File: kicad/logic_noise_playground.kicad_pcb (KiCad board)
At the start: 2 copper layers, 200 x 100 mm, 160 parts, among them J2 SJ1-3524NG, P1 CONN_02X03, P10 CONN_01X03, P11 CONN_01X05, P12 CONN_02X04, P13 CONN_01X03, P14 CONN_01X02, P15 CONN_02X08, P16 CONN_01X04, P17 CONN_02X04, P18 CONN_01X04, P19 CONN_01X02, P2 CONN_01X02, P20 CONN_01X06, P21 CONN_02X03, P22 CONN_02X03, P23 CONN_01X02, P24 CONN_02X01, P25 CONN_01X02, P26 CONN_02X12, P27 CONN_01X02, P28 CONN_01X02, P29 CONN_01X02, P3 CONN_02X02, P30 CONN_01X02, P31 CONN_01X02, P32 CONN_01X03, P33 CONN_01X04, P34 CONN_01X04, P35 CONN_01X04, P36 CONN_01X04, P37 CONN_02X01, P38 CONN_01X04, P39 CONN_01X04, P4 CONN_02X06, P40 CONN_01X02, P5 CONN_02X02, P6 4017 Outs, P7 CONN_01X08, P8 CONN_02X03, P9 CONN_01X08, Q1 LM3904, SW1 Set, SW2 Clear, U1 40106, U2 4070, U3 40106, U4 4069, U5 4051, U6 4015, U7 4017, U8 4040

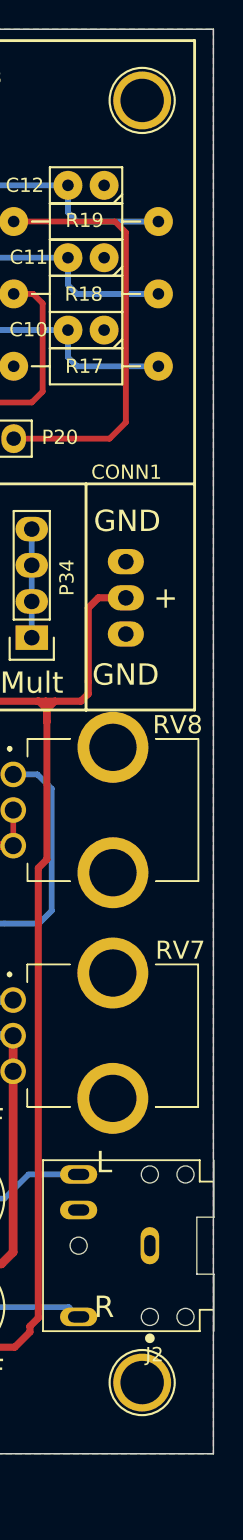
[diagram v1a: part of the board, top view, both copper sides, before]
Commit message: update reference number output
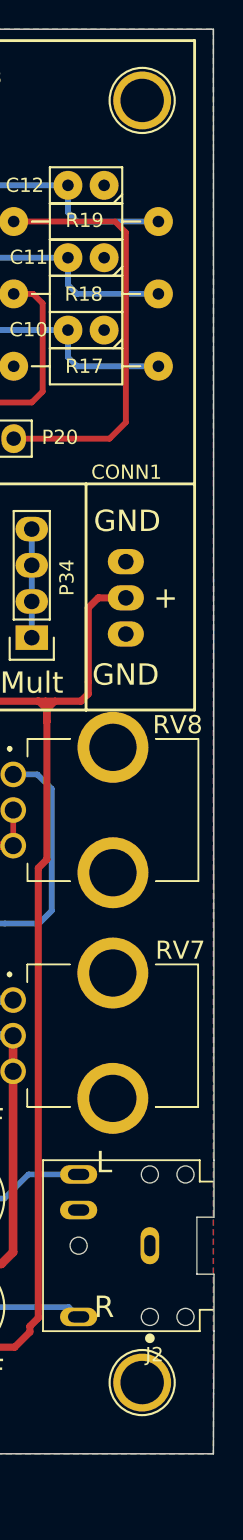
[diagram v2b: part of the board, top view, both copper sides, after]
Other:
- outline, holes or cut-outs redrawn
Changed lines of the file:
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@@
 		(allow_soldermask_bridges_in_footprints no)
 		(pcbplotparams
-			(layerselection 0x00330f0_80000001)
+			(layerselection 0x00330f0_ffffffff)
 			(plot_on_all_layers_selection 0x0001000_00000000)
 			(disableapertmacros no)
@@
 			(psnegative no)
 			(psa4output no)
-			(plotreference no)
+			(plotreference yes)
 			(plotvalue no)
 			(plotfptext yes)
@@
 			(drillshape 0)
 			(scaleselection 1)
-			(outputdirectory "")
+			(outputdirectory "gerbers/")
 		)
 	)
@@
 			)
 		)
-		(sheetname "Raíz")
-		(sheetfile "logic_noise_playground.kicad_sch")
 		(attr through_hole)
 		(fp_line
@@
 			(end -4.5 6)
 			(stroke
-				(width 0.01)
+				(width 0.1)
 				(type solid)
 			)
@@
 			(end -4.5 -2)
 			(stroke
-				(width 0.01)
+				(width 0.1)
 				(type solid)
 			)
@@
 	)
 	(gr_line
+		(start 235.04 141.39)
+		(end 235 150)
+		(stroke
+			(width 0.1)
+			(type default)
+		)
+		(layer "Edge.Cuts")
+	)
+	(gr_line
 		(start 35 150)
 		(end 235 150)
@@
 	)
 	(gr_line
-		(start 235 150)
+		(start 235.04 129.39)
 		(end 235 50)
 		(stroke

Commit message: update gerbers
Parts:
- removed the G*** at (137.2, 100.3)
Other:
- board text removed: "Layout and Logic: Elliot Williams"
- board text removed: "https://hackaday.com/tag/logic-noise"
